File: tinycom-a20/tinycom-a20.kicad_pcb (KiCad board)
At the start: 4 copper layers, 41.7 x 40.9 mm, 37 parts, among them P1 CONN_02X10, P2 CONN_02X10, P3 CONN_01X01, P4 CONN_01X03, U1 ALLWINNERA10/TFBGA441, U2 H5TQG63BFR/FBGA96, Y1 Crystal_Small, Y2 Crystal_Small

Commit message: pics
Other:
- rule pad_to_mask_clearance: 0.07 -> 0.065

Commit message: before test axp209
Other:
- net class Default: trace_width 0.15 -> 0.14
- net class Ground: trace_width 0.15 -> 0.14
- net class Power: trace_width 0.15 -> 0.14

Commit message: fix a20
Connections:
- P1 pad 1: (no net) -> HTX2P
- P1 pad 11: (no net) -> HTX0N
- P1 pad 13: (no net) -> HTXCP
- P1 pad 15: (no net) -> HTXCN
- P1 pad 16: (no net) -> MICIN1
- P1 pad 17: (no net) -> HCEC
- P1 pad 18: (no net) -> HHPD
- P1 pad 19: (no net) -> HSCL
- P1 pad 20: (no net) -> HSDA
- P1 pad 3: (no net) -> HTX2N
- P1 pad 4: (no net) -> UART1_TX
- P1 pad 5: (no net) -> HTX1P
- P1 pad 6: (no net) -> UART1_RX
- P1 pad 7: (no net) -> HTX1N
- P1 pad 9: (no net) -> HTX0P
- P2 pad 13: (no net) -> Net-(P2-Pad13)
- P2 pad 15: (no net) -> Net-(P2-Pad15)
- P2 pad 17: (no net) -> Net-(P2-Pad17)
- P2 pad 8: (no net) -> Net-(P2-Pad8)
- U1 pad A1: (no net) -> Net-(U1-PadA1)
- U1 pad A10: (no net) -> Net-(U1-PadA10)
- U1 pad A11: (no net) -> Net-(U1-PadA11)
- U1 pad A12: (no net) -> Net-(U1-PadA12)
- U1 pad A13: (no net) -> Net-(U1-PadA13)
- U1 pad A14: (no net) -> Net-(U1-PadA14)
- U1 pad A16: (no net) -> Net-(U1-PadA16)
- U1 pad A17: (no net) -> Net-(U1-PadA17)
- U1 pad A18: (no net) -> Net-(U1-PadA18)
- U1 pad A19: (no net) -> Net-(U1-PadA19)
- U1 pad A2: (no net) -> Net-(U1-PadA2)
- U1 pad A20: (no net) -> Net-(U1-PadA20)
- U1 pad A21: (no net) -> Net-(U1-PadA21)
- U1 pad A22: (no net) -> Net-(U1-PadA22)
- U1 pad A23: (no net) -> Net-(U1-PadA23)
- U1 pad A3: (no net) -> Net-(U1-PadA3)
- U1 pad A4: (no net) -> Net-(U1-PadA4)
- U1 pad A5: (no net) -> Net-(U1-PadA5)
- U1 pad A6: (no net) -> Net-(U1-PadA6)
- U1 pad A8: (no net) -> Net-(U1-PadA8)
- U1 pad A9: (no net) -> Net-(U1-PadA9)
- U1 pad AA10: (no net) -> Net-(U1-PadAA10)
- U1 pad AA11: (no net) -> Net-(U1-PadAA11)
- U1 pad AA12: (no net) -> Net-(U1-PadAA12)
- U1 pad AA13: (no net) -> Net-(U1-PadAA13)
- U1 pad AA14: (no net) -> Net-(U1-PadAA14)
- U1 pad AA15: (no net) -> Net-(U1-PadAA15)
- U1 pad AA16: (no net) -> Net-(U1-PadAA16)
- U1 pad AA17: (no net) -> Net-(U1-PadAA17)
- U1 pad AA19: (no net) -> Net-(U1-PadAA19)
- U1 pad AA20: (no net) -> Net-(U1-PadAA20)
- U1 pad AA21: (no net) -> Net-(U1-PadAA21)
- U1 pad AA22: (no net) -> Net-(U1-PadAA22)
- U1 pad AA23: (no net) -> Net-(U1-PadAA23)
- U1 pad AA4: (no net) -> Net-(U1-PadAA4)
- U1 pad AA9: (no net) -> Net-(U1-PadAA9)
- U1 pad AB10: (no net) -> Net-(U1-PadAB10)
- U1 pad AB11: (no net) -> Net-(U1-PadAB11)
- U1 pad AB12: (no net) -> Net-(U1-PadAB12)
- U1 pad AB13: (no net) -> Net-(U1-PadAB13)
- U1 pad AB14: (no net) -> Net-(U1-PadAB14)
- U1 pad AB15: (no net) -> Net-(U1-PadAB15)
- U1 pad AB16: (no net) -> Net-(U1-PadAB16)
- U1 pad AB17: (no net) -> Net-(U1-PadAB17)
- U1 pad AB18: (no net) -> Net-(U1-PadAB18)
- U1 pad AB19: (no net) -> VCC_33
- U1 pad AB20: (no net) -> Net-(U1-PadAB20)
- U1 pad AB21: (no net) -> Net-(U1-PadAB21)
- U1 pad AB22: (no net) -> Net-(U1-PadAB22)
- U1 pad AB23: (no net) -> Net-(U1-PadAB23)
- U1 pad AB9: (no net) -> Net-(U1-PadAB9)
- U1 pad AC10: (no net) -> Net-(U1-PadAC10)
- U1 pad AC11: (no net) -> Net-(U1-PadAC11)
- U1 pad AC12: (no net) -> Net-(U1-PadAC12)
- U1 pad AC13: (no net) -> Net-(U1-PadAC13)
- U1 pad AC14: (no net) -> Net-(U1-PadAC14)
- U1 pad AC15: (no net) -> Net-(U1-PadAC15)
- U1 pad AC16: (no net) -> Net-(U1-PadAC16)
- U1 pad AC17: (no net) -> Net-(U1-PadAC17)
- U1 pad AC18: (no net) -> Net-(U1-PadAC18)
- U1 pad AC20: (no net) -> Net-(U1-PadAC20)
- U1 pad AC21: (no net) -> Net-(U1-PadAC21)
- U1 pad AC22: (no net) -> Net-(U1-PadAC22)
- U1 pad AC23: (no net) -> Net-(U1-PadAC23)
- U1 pad AC9: (no net) -> Net-(U1-PadAC9)
- U1 pad B1: (no net) -> Net-(U1-PadB1)
- U1 pad B10: (no net) -> Net-(U1-PadB10)
- U1 pad B11: (no net) -> Net-(U1-PadB11)
- U1 pad B12: (no net) -> Net-(U1-PadB12)
- U1 pad B13: (no net) -> Net-(U1-PadB13)
- U1 pad B14: (no net) -> Net-(U1-PadB14)
- U1 pad B16: (no net) -> Net-(U1-PadB16)
- U1 pad B17: (no net) -> Net-(U1-PadB17)
- U1 pad B18: (no net) -> Net-(U1-PadB18)
- U1 pad B19: (no net) -> Net-(U1-PadB19)
- U1 pad B2: (no net) -> Net-(U1-PadB2)
- U1 pad B20: (no net) -> Net-(U1-PadB20)
- U1 pad B21: (no net) -> Net-(U1-PadB21)
- U1 pad B22: (no net) -> Net-(U1-PadB22)
- U1 pad B23: (no net) -> Net-(U1-PadB23)
- U1 pad B3: (no net) -> Net-(U1-PadB3)
- U1 pad B4: (no net) -> Net-(U1-PadB4)
- U1 pad B5: (no net) -> Net-(U1-PadB5)
- U1 pad B6: (no net) -> Net-(U1-PadB6)
- U1 pad B8: (no net) -> Net-(U1-PadB8)
- U1 pad B9: (no net) -> Net-(U1-PadB9)
- U1 pad C1: (no net) -> Net-(U1-PadC1)
- U1 pad C10: (no net) -> Net-(U1-PadC10)
- U1 pad C11: (no net) -> Net-(U1-PadC11)
- U1 pad C12: (no net) -> Net-(U1-PadC12)
- U1 pad C13: (no net) -> Net-(U1-PadC13)
- U1 pad C15: (no net) -> Net-(U1-PadC15)
- U1 pad C16: (no net) -> Net-(U1-PadC16)
- U1 pad C17: (no net) -> Net-(U1-PadC17)
- U1 pad C18: (no net) -> Net-(U1-PadC18)
- U1 pad C19: (no net) -> Net-(U1-PadC19)
- U1 pad C2: (no net) -> Net-(U1-PadC2)
- U1 pad C20: (no net) -> Net-(U1-PadC20)
- U1 pad C21: (no net) -> Net-(U1-PadC21)
- U1 pad C22: (no net) -> Net-(U1-PadC22)
- U1 pad C23: (no net) -> Net-(U1-PadC23)
- U1 pad C3: (no net) -> Net-(U1-PadC3)
- U1 pad C4: (no net) -> Net-(U1-PadC4)
- U1 pad C5: (no net) -> Net-(U1-PadC5)
- U1 pad C6: (no net) -> Net-(U1-PadC6)
- U1 pad C7: (no net) -> Net-(U1-PadC7)
- U1 pad C8: (no net) -> Net-(U1-PadC8)
- U1 pad C9: (no net) -> Net-(U1-PadC9)
- U1 pad D1: (no net) -> Net-(U1-PadD1)
- U1 pad D10: (no net) -> Net-(U1-PadD10)
- U1 pad D11: (no net) -> Net-(U1-PadD11)
- U1 pad D12: (no net) -> Net-(U1-PadD12)
- U1 pad D13: (no net) -> Net-(U1-PadD13)
- U1 pad D14: (no net) -> Net-(U1-PadD14)
- U1 pad D15: (no net) -> Net-(U1-PadD15)
- U1 pad D16: (no net) -> Net-(U1-PadD16)
- U1 pad D17: (no net) -> Net-(U1-PadD17)
- U1 pad D18: (no net) -> Net-(U1-PadD18)
- U1 pad D19: (no net) -> Net-(U1-PadD19)
- U1 pad D2: (no net) -> Net-(U1-PadD2)
- U1 pad D20: (no net) -> Net-(U1-PadD20)
- U1 pad D21: (no net) -> Net-(U1-PadD21)
- U1 pad D22: (no net) -> Net-(U1-PadD22)
- U1 pad D23: (no net) -> Net-(U1-PadD23)
- U1 pad D3: (no net) -> Net-(U1-PadD3)
- U1 pad D4: (no net) -> Net-(U1-PadD4)
- U1 pad D5: (no net) -> Net-(U1-PadD5)
- U1 pad D6: (no net) -> Net-(U1-PadD6)
- U1 pad D7: (no net) -> Net-(U1-PadD7)
- U1 pad D8: (no net) -> Net-(U1-PadD8)
- U1 pad D9: (no net) -> Net-(U1-PadD9)
- U1 pad E1: (no net) -> Net-(U1-PadE1)
- U1 pad E10: (no net) -> Net-(U1-PadE10)
- U1 pad E11: (no net) -> Net-(U1-PadE11)
- U1 pad E12: (no net) -> Net-(U1-PadE12)
- U1 pad E13: (no net) -> Net-(U1-PadE13)
- U1 pad E14: (no net) -> Net-(U1-PadE14)
- U1 pad E15: (no net) -> Net-(U1-PadE15)
- U1 pad E16: (no net) -> Net-(U1-PadE16)
- U1 pad E17: (no net) -> Net-(U1-PadE17)
- U1 pad E18: (no net) -> Net-(U1-PadE18)
- U1 pad E19: (no net) -> Net-(U1-PadE19)
- U1 pad E2: (no net) -> Net-(U1-PadE2)
- U1 pad E20: (no net) -> Net-(U1-PadE20)
- U1 pad E21: (no net) -> Net-(U1-PadE21)
- U1 pad E22: (no net) -> Net-(U1-PadE22)
- U1 pad E23: (no net) -> Net-(U1-PadE23)
- U1 pad E3: (no net) -> Net-(U1-PadE3)
- U1 pad E4: (no net) -> Net-(U1-PadE4)
- U1 pad E5: (no net) -> Net-(U1-PadE5)
- U1 pad E6: (no net) -> Net-(U1-PadE6)
- U1 pad E7: (no net) -> Net-(U1-PadE7)
- U1 pad E8: (no net) -> Net-(U1-PadE8)
- U1 pad E9: (no net) -> Net-(U1-PadE9)
- U1 pad F19: (no net) -> Net-(U1-PadF19)
- U1 pad F20: (no net) -> Net-(U1-PadF20)
- U1 pad F21: (no net) -> Net-(U1-PadF21)
- U1 pad F22: (no net) -> Net-(U1-PadF22)
- U1 pad F23: (no net) -> Net-(U1-PadF23)
- U1 pad F3: (no net) -> Net-(U1-PadF3)
- U1 pad F4: (no net) -> Net-(U1-PadF4)
- U1 pad G1: (no net) -> SDQM3
- U1 pad G19: (no net) -> Net-(U1-PadG19)
- U1 pad G2: (no net) -> SDQ30
- U1 pad G20: (no net) -> ND7
- U1 pad G21: (no net) -> ND6
- U1 pad G22: (no net) -> ND3
- U1 pad G23: (no net) -> ND2
- U1 pad H1: (no net) -> SDQ25
- U1 pad H2: (no net) -> SDQ27
- U1 pad H20: (no net) -> ND5
- U1 pad H21: (no net) -> ND4
- U1 pad H22: (no net) -> ND1
- U1 pad H23: (no net) -> ND0
- U1 pad J1: (no net) -> SDQ28
- U1 pad J2: (no net) -> SDQS3_N
- U1 pad J20: (no net) -> Net-(U1-PadJ20)
- U1 pad J21: (no net) -> Net-(U1-PadJ21)
- U1 pad J22: (no net) -> Net-(U1-PadJ22)
- U1 pad J23: (no net) -> NRB0
- U1 pad J3: (no net) -> Net-(U1-PadJ3)
- U1 pad J4: (no net) -> Net-(U1-PadJ4)
- U1 pad K1: (no net) -> SDQS3_P
- U1 pad K2: (no net) -> SDQ31
- U1 pad K21: (no net) -> Net-(U1-PadK21)
- U1 pad K22: (no net) -> NRE#
- U1 pad K23: (no net) -> NCE0
- U1 pad L1: (no net) -> SDQ24
- U1 pad L2: (no net) -> SDQ26
- U1 pad L21: (no net) -> Net-(U1-PadL21)
- U1 pad L22: (no net) -> Net-(U1-PadL22)
- U1 pad L23: (no net) -> NCLE
- U1 pad M1: (no net) -> SDQ29
- U1 pad M2: (no net) -> SDQ23
- U1 pad M21: (no net) -> Net-(U1-PadM21)
- U1 pad M22: (no net) -> NALE
- U1 pad M23: (no net) -> NWE#
- U1 pad N1: (no net) -> SDQ16
- U1 pad N15: (no net) -> Net-(U1-PadN15)
- U1 pad N16: (no net) -> Net-(U1-PadN16)
- U1 pad N2: (no net) -> SDQ18
- U1 pad N8: (no net) -> Net-(U1-PadN8)
- U1 pad P1: (no net) -> SDQ21
- U1 pad P19: (no net) -> Net-(U1-PadP19)
- U1 pad P2: (no net) -> SDQS2_N
- U1 pad P22: (no net) -> Net-(U1-PadP22)
- U1 pad P23: (no net) -> Net-(U1-PadP23)
- U1 pad P8: (no net) -> Net-(U1-PadP8)
- U1 pad R1: (no net) -> SDQS2_P
- U1 pad R14: (no net) -> Net-(U1-PadR14)
- U1 pad R15: (no net) -> Net-(U1-PadR15)
- U1 pad R16: (no net) -> Net-(U1-PadR16)
- U1 pad R19: (no net) -> Net-(U1-PadR19)
- U1 pad R2: (no net) -> SDQM2
- U1 pad R20: (no net) -> UD2_N
- U1 pad R21: (no net) -> UD2_P
- U1 pad R22: (no net) -> Net-(U1-PadR22)
- U1 pad R23: (no net) -> Net-(U1-PadR23)
- U1 pad R8: (no net) -> Net-(U1-PadR8)
- U1 pad T1: (no net) -> SDQ22
- U1 pad T14: (no net) -> Net-(U1-PadT14)
- U1 pad T15: (no net) -> Net-(U1-PadT15)
- U1 pad T16: (no net) -> Net-(U1-PadT16)
- U1 pad T2: (no net) -> SDQ17
- U1 pad T20: (no net) -> Net-(U1-PadT20)
- U1 pad T21: (no net) -> Net-(U1-PadT21)
- U1 pad T22: (no net) -> Net-(U1-PadT22)
- U1 pad T23: (no net) -> Net-(U1-PadT23)
- U1 pad U1: (no net) -> SDQ19
- U1 pad U2: (no net) -> SDQ20
- U1 pad U20: (no net) -> Net-(U1-PadU20)
- U1 pad U21: (no net) -> Net-(U1-PadU21)
- U1 pad U22: (no net) -> Net-(U1-PadU22)
- U1 pad U23: (no net) -> Net-(U1-PadU23)
- U1 pad V20: (no net) -> Net-(U1-PadV20)
- U1 pad V21: (no net) -> Net-(U1-PadV21)
- U1 pad V22: (no net) -> Net-(U1-PadV22)
- U1 pad V23: (no net) -> Net-(U1-PadV23)
- U1 pad W17: (no net) -> Net-(U1-PadW17)
- U1 pad W19: (no net) -> Net-(U1-PadW19)
- U1 pad W20: (no net) -> Net-(U1-PadW20)
- U1 pad W21: (no net) -> Net-(U1-PadW21)
- U1 pad W22: (no net) -> Net-(U1-PadW22)
- U1 pad W23: (no net) -> Net-(U1-PadW23)
- U1 pad Y10: (no net) -> Net-(U1-PadY10)
- U1 pad Y11: (no net) -> Net-(U1-PadY11)
- U1 pad Y12: (no net) -> Net-(U1-PadY12)
- U1 pad Y13: (no net) -> Net-(U1-PadY13)
- U1 pad Y14: (no net) -> Net-(U1-PadY14)
- U1 pad Y15: (no net) -> Net-(U1-PadY15)
- U1 pad Y16: (no net) -> Net-(U1-PadY16)
- U1 pad Y17: (no net) -> Net-(U1-PadY17)
- U1 pad Y19: (no net) -> Net-(U1-PadY19)
- U1 pad Y20: (no net) -> Net-(U1-PadY20)
- U1 pad Y21: (no net) -> Net-(U1-PadY21)
- U1 pad Y22: (no net) -> Net-(U1-PadY22)
- U1 pad Y23: (no net) -> Net-(U1-PadY23)
- U1 pad Y9: (no net) -> Net-(U1-PadY9)
- U2 pad J1: (no net) -> Net-(U2-PadJ1)
- U2 pad J9: (no net) -> Net-(U2-PadJ9)
- U2 pad L1: (no net) -> Net-(U2-PadL1)
- U2 pad L9: (no net) -> Net-(U2-PadL9)
- U2 pad M7: (no net) -> Net-(U2-PadM7)
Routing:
- net VCC_33: track 53.6 -> 58.7 mm, vias 11 -> 12
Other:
- net class Power: trace_width 0.14 -> 0.3

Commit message: add video
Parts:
- moved C2 8.76 mm to (124.7, 135.8), turned to 90 degrees
- moved C1 8.66 mm to (124.7, 144.5), turned to 270 degrees
- moved P3 6.18 mm to (112.4, 151.1)
- moved C17 3.90 mm to (115.8, 147.9)
- moved Y1 0.11 mm to (124.4, 140.2), turned to 270 degrees
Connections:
- P1 pad 1: HTX2P -> HTX2_P
- P1 pad 10: UD0_N -> UD1_N
- P1 pad 11: HTX0N -> HTX0_N
- P1 pad 12: UD1_P -> MICIN1
- P1 pad 13: HTXCP -> HTXC_P
- P1 pad 14: UD1_N -> HPOUTL
- P1 pad 15: HTXCN -> HTXC_N
- P1 pad 16: MICIN1 -> HPOUTR
- P1 pad 3: HTX2N -> HTX2_N
- P1 pad 4: UART1_TX -> UD0_P
- P1 pad 5: HTX1P -> HTX1_P
- P1 pad 6: UART1_RX -> UD0_N
- P1 pad 7: HTX1N -> HTX1_N
- P1 pad 8: UD0_P -> UD1_P
- P1 pad 9: HTX0P -> HTX0_P
- P2 pad 15: Net-(P2-Pad15) -> UART1_RX
- P2 pad 17: Net-(P2-Pad17) -> UART1_TX
- U1 pad AC20: Net-(U1-PadAC20) -> MICIN1
- U1 pad P22: Net-(U1-PadP22) -> HHPD
- U1 pad P23: Net-(U1-PadP23) -> HCEC
- U1 pad R22: Net-(U1-PadR22) -> HSDA
- U1 pad R23: Net-(U1-PadR23) -> HSCL
- U1 pad T22: Net-(U1-PadT22) -> HTX2_N
- U1 pad T23: Net-(U1-PadT23) -> HTX2_P
- U1 pad U22: Net-(U1-PadU22) -> HTX1_N
- U1 pad U23: Net-(U1-PadU23) -> HTX1_P
- U1 pad V22: Net-(U1-PadV22) -> HTX0_N
- U1 pad V23: Net-(U1-PadV23) -> HTX0_P
- U1 pad W19: Net-(U1-PadW19) -> HPOUTR
- U1 pad W22: Net-(U1-PadW22) -> HTXC_N
- U1 pad W23: Net-(U1-PadW23) -> HTXC_P
- U1 pad Y19: Net-(U1-PadY19) -> HPOUTL
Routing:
- net HTX2_P: track 0.00 -> 36.0 mm, vias 0 -> 1
- net HTX2_N: track 0.00 -> 33.7 mm, vias 0 -> 1
- net HTX1_P: track 0.00 -> 30.0 mm, vias 0 -> 1
- net HTX1_N: track 0.00 -> 28.7 mm, vias 0 -> 1
- net HTX0_P: track 0.00 -> 26.2 mm, vias 0 -> 1
- net HHPD: track 0.00 -> 25.2 mm, vias 0 -> 1
- net HSDA: track 0.00 -> 24.2 mm, vias 0 -> 1
- net HTX0_N: track 0.00 -> 23.3 mm, vias 0 -> 1
- net HCEC: track 0.00 -> 20.8 mm, vias 0 -> 1
- net HTXC_P: track 0.00 -> 20.2 mm, vias 0 -> 1
- net HSCL: track 0.00 -> 19.8 mm, vias 0 -> 1
- net HPOUTR: track 0.00 -> 19.5 mm
- net HPOUTL: track 0.00 -> 19.3 mm
- net MICIN1: track 0.00 -> 18.1 mm
- net HTXC_N: track 0.00 -> 17.4 mm, vias 0 -> 1
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
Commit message: readme
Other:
- rule pad_to_mask_clearance: 0.065 -> 0.07
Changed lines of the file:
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@@
   (general
     (links 294)
-    (no_connects 7)
-    (area 84.124999 120.824999 125.975001 161.875001)
+    (no_connects 0)
+    (area 79.915 117.446666 127.515 162.603333)
     (thickness 1.6)
     (drawings 20)
@@
     (pad_size 0.35 0.35)
     (pad_drill 0)
-    (pad_to_mask_clearance 0.065)
+    (pad_to_mask_clearance 0.07)
     (aux_axis_origin 0 0)
     (grid_origin 80.98 162.84)

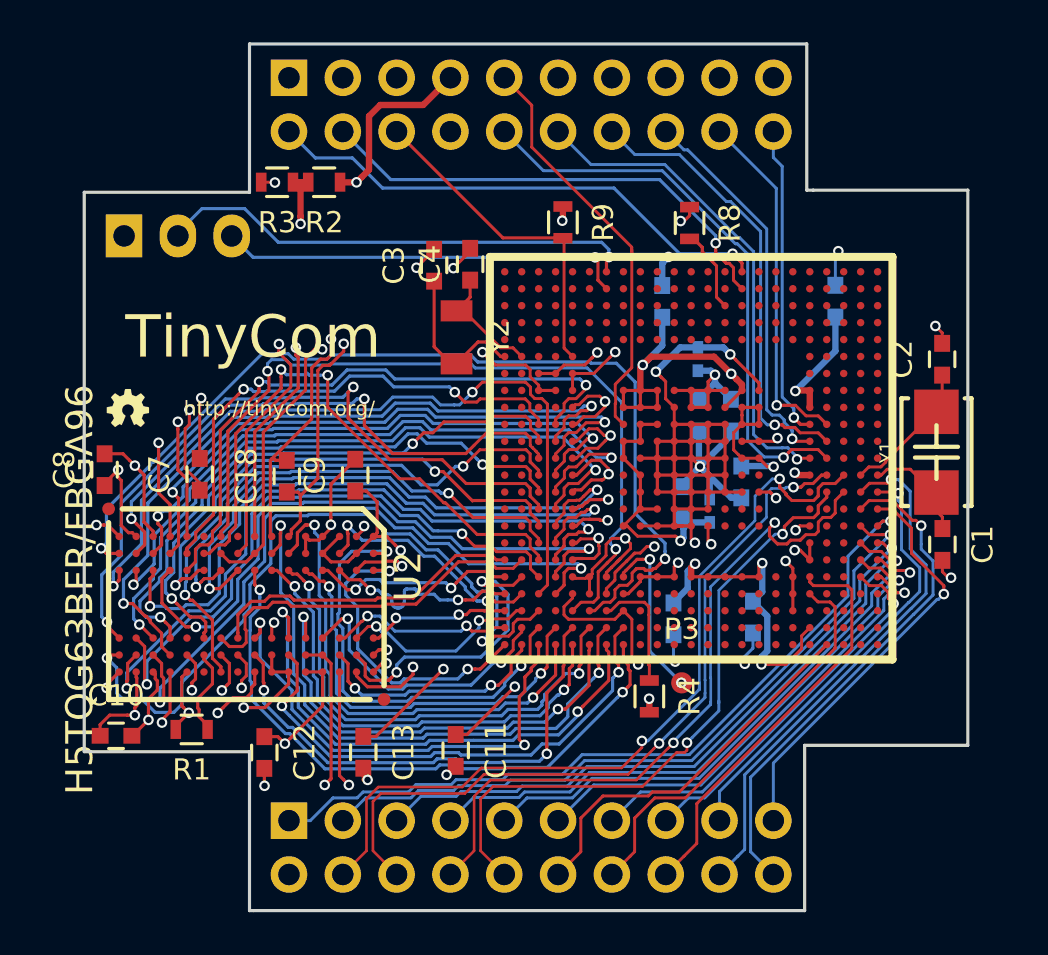
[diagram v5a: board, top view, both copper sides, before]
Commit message: update a20+base (connect reset)
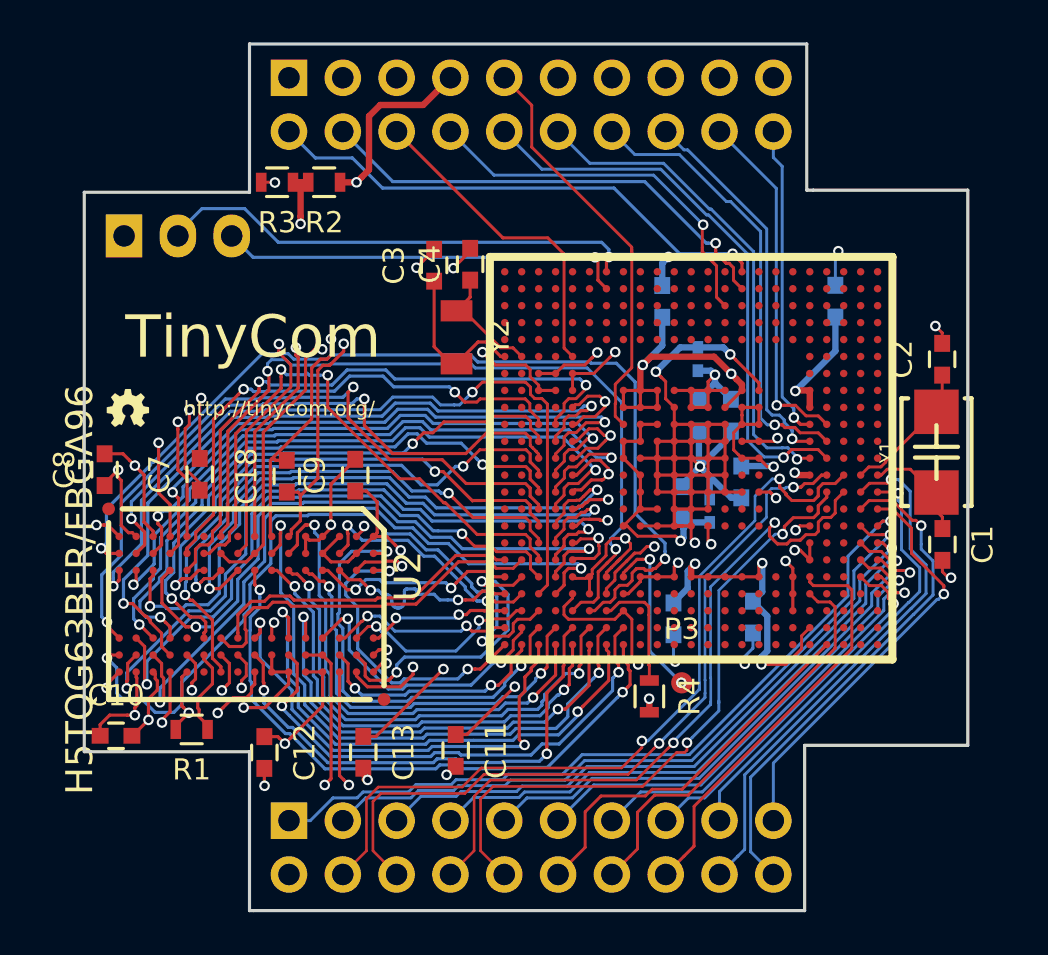
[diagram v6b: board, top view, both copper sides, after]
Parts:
- removed R8, R9: 47K, Resistors_SMD:R_0603
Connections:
- net Net-(P2-Pad13) renamed LDO3_28
- net UART1_RX renamed LDO4_28
- net UART1_TX renamed Net-(P2-Pad17)
- P2 pad 8: Net-(P2-Pad8) -> RESET_N
- U1 pad C14: RESET# -> RESET_N
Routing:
- net RESET_N: track 0.00 -> 18.0 mm, vias 0 -> 1
- net RESET#: track 3.96 -> 0.00 mm
- net VCC_33: track 58.1 -> 56.5 mm, vias 12 -> 10

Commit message: add ground fg/bg to a20
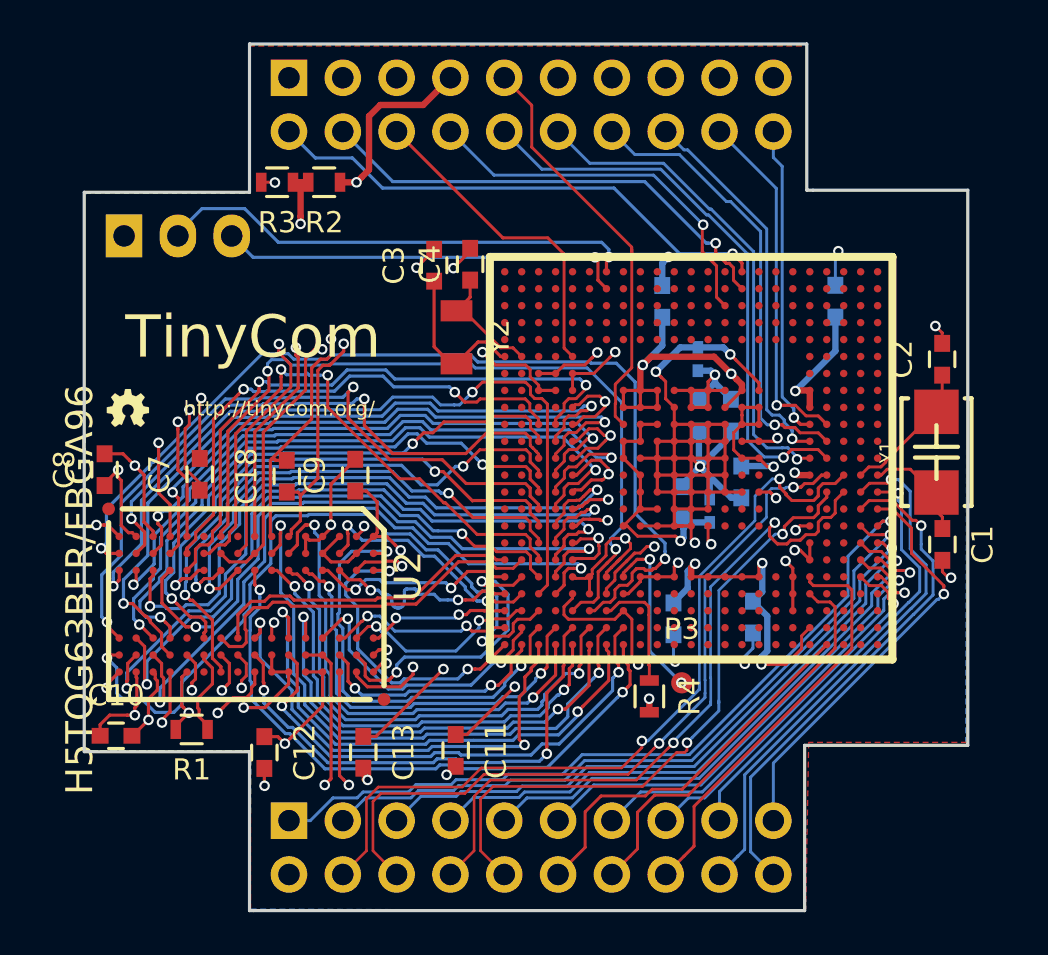
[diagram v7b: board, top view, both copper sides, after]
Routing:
- added copper zone on B.Cu, net GND
- added copper zone on F.Cu, net GND
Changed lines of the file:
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@@
+    )
+  )
+  (zone (net 23) (net_name GND) (layer F.Cu) (hatch edge 0.508)
+    (connect_pads (clearance 0.1))
+    (min_thickness 0.254)
+    (fill yes (arc_segments 16) (thermal_gap 0.508) (thermal_bridge_width 0.508))
+    (polygon
+      (pts
+        (xy 84.21 127.91) (xy 91.96 127.91) (xy 91.96 121) (xy 118.26 121) (xy 118.26 127.78)
+        (xy 125.86 127.8) (xy 125.86 153.86) (xy 118.39 153.86) (xy 118.25 161.76) (xy 92.05 161.76)
+        (xy 92.05 154.26) (xy 84.25 154.26) (xy 84.25 128.01) (xy 84.26 128)
+      )
+    )
+  )
+  (zone (net 23) (net_name GND) (layer B.Cu) (hatch edge 0.508)
+    (connect_pads (clearance 0.1))
+    (min_thickness 0.254)
+    (fill yes (arc_segments 16) (thermal_gap 0.508) (thermal_bridge_width 0.508))
+    (polygon
+      (pts
+        (xy 84.26 127.93) (xy 92.01 127.93) (xy 92.01 120.94) (xy 118.26 120.94) (xy 118.26 127.78)
+        (xy 125.88 127.78) (xy 125.8 154.02) (xy 118.18 153.98) (xy 118.16 161.82) (xy 92 161.73)
+        (xy 92.07 154.27) (xy 84.23 154.27) (xy 84.23 128.03) (xy 84.29 127.97)
+      )
     )
   )

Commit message: a20 remove bottom components
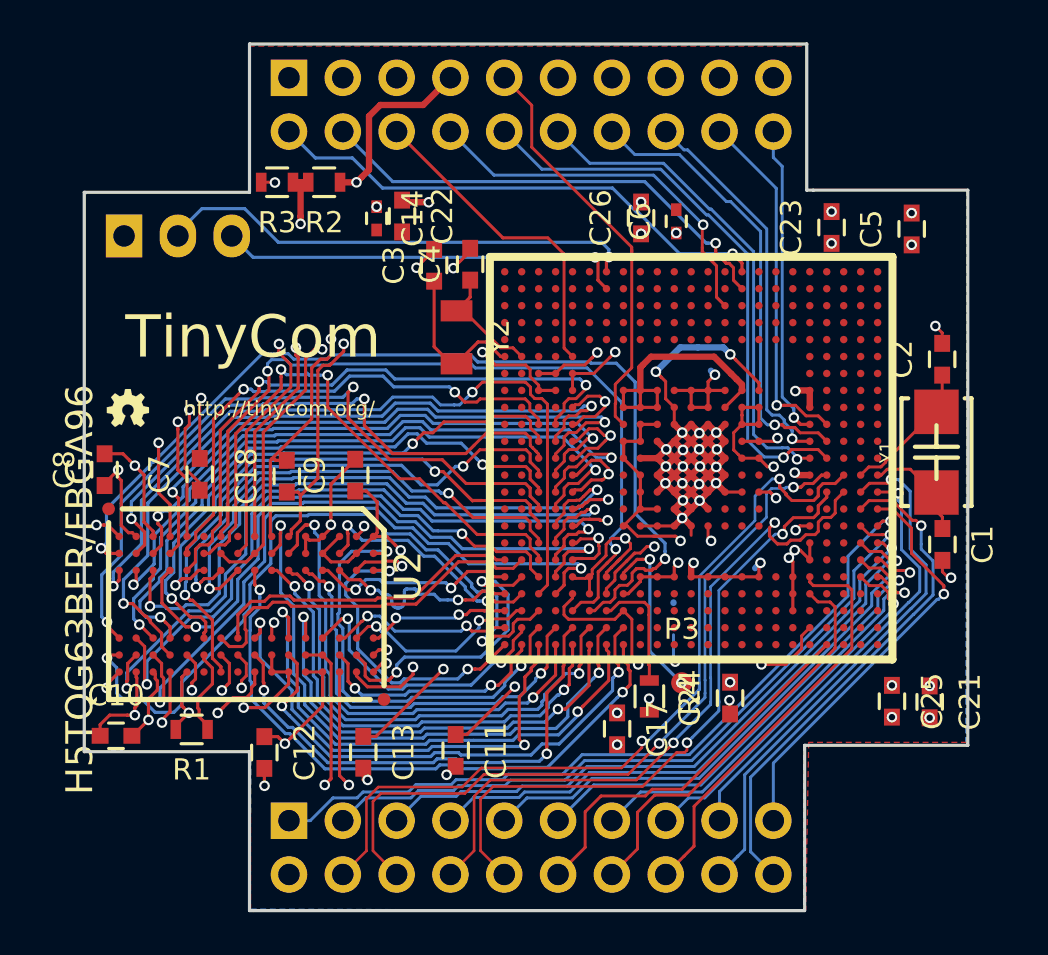
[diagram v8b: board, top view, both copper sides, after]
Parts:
- C14, C17, C21, C22, C23, C24, C25, C26, C5, C6: moved to F.Cu
- moved C14 20.9 mm to (98.0, 129.1), turned to 270 degrees
- moved C22 18.1 mm to (99.2, 129.0)
- moved C21 12.7 mm to (124.1, 151.9)
- moved C25 12.6 mm to (122.3, 151.9)
- moved C23 10.8 mm to (119.5, 129.6), turned to 90 degrees
- moved C24 9.49 mm to (114.7, 151.8), turned to 90 degrees
- moved C17 8.30 mm to (109.3, 153.2)
- moved C6 6.58 mm to (112.1, 129.3)
- moved C5 4.96 mm to (123.2, 129.6)
- moved C26 4.06 mm to (110.5, 129.1)
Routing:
- net VCC_12_INT: track 60.5 -> 80.9 mm, vias 2 -> 5
- net VCC_12_CPU: track 38.8 -> 54.6 mm, vias 1 -> 4
- net VCC_33: track 56.5 -> 42.1 mm, vias 10 -> 12
- net GND: track 179.1 -> 168.3 mm, vias 42 -> 61
- net (no net): track 0.00 -> 1.33 mm, vias 0 -> 1
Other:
- net class Ground: trace_width 0.14 -> 0.3
